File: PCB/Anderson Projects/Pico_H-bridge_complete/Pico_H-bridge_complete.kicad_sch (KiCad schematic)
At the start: 43 parts, among them J1 Screw_Terminal_01x9, J2 Motor Connector, J3 Screw_Terminal_01x02, SW1 SW_DIP_x01, U1 Pico, U11 MCP6001R, U5 OPA4197

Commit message: Gerber files for Pico_H-bridge_complete v1 generated
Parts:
- removed TP10: B, TestPoint:TestPoint_Plated_Hole_D2.0mm, symbol Connector:TestPoint
- removed TP7: Limit, TestPoint:TestPoint_Plated_Hole_D2.0mm, symbol Connector:TestPoint
- removed TP8: Home, TestPoint:TestPoint_Plated_Hole_D2.0mm, symbol Connector:TestPoint
- removed TP9: A, TestPoint:TestPoint_Plated_Hole_D2.0mm, symbol Connector:TestPoint
- D1: footprint LED_SMD:LED_0603_1608Metric -> LED_SMD:LED_0805_2012Metric; LCSC C2286 -> C2296
- D2: footprint LED_SMD:LED_0603_1608Metric -> LED_SMD:LED_0805_2012Metric; LCSC C2290 -> C34499
- J1: footprint TerminalBlock_Phoenix:TerminalBlock_Phoenix_PT-1,5-10-5.0-H_1x10_P5.00mm_Horizontal -> TerminalBlock_Phoenix:TerminalBlock_Phoenix_PT-1,5-9-5.0-H_1x09_P5.00mm_Horizontal
- R1, R2: footprint Resistor_SMD:R_0603_1608Metric -> Resistor_SMD:R_0805_2012Metric_Pad1.20x1.40mm_HandSolder
- R10, R4, R6: footprint Resistor_SMD:R_0603_1608Metric -> Resistor_SMD:R_0805_2012Metric_Pad1.20x1.40mm_HandSolder; LCSC C23018 -> C17614
- R11, R17: footprint Resistor_SMD:R_0603_1608Metric -> Resistor_SMD:R_0805_2012Metric_Pad1.20x1.40mm_HandSolder; LCSC C23186 -> C27834
- R12, R13, R15, R16, R18, R19: footprint Resistor_SMD:R_0603_1608Metric -> Resistor_SMD:R_0805_2012Metric_Pad1.20x1.40mm_HandSolder; LCSC C25804 -> C17414
- R14: footprint Resistor_SMD:R_0603_1608Metric -> Resistor_SMD:R_0805_2012Metric_Pad1.20x1.40mm_HandSolder; LCSC C25819 -> C17713
- R20, R21: footprint Resistor_SMD:R_0603_1608Metric -> Resistor_SMD:R_0805_2012Metric_Pad1.20x1.40mm_HandSolder; LCSC C22978 -> C26010
- R24: footprint Resistor_SMD:R_0603_1608Metric -> Resistor_SMD:R_0805_2012Metric_Pad1.20x1.40mm_HandSolder; LCSC C4260 -> C17767
- R25: footprint Resistor_SMD:R_0603_1608Metric -> Resistor_SMD:R_0805_2012Metric_Pad1.20x1.40mm_HandSolder; LCSC C22797 -> C17455
- R3, R5: footprint Resistor_SMD:R_0603_1608Metric -> Resistor_SMD:R_0805_2012Metric_Pad1.20x1.40mm_HandSolder; LCSC C4177 -> C17398
- U11: LCSC (none) -> C154973

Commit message: Anderson Motor Interface Board v2 complete and ordered.
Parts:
- removed D14: 5.1V, Diode_SMD:D_SOD-323, symbol Diode:Z1SMAxxx
- added R32: 82k, Resistor_SMD:R_0805_2012Metric_Pad1.20x1.40mm_HandSolder, symbol Device:R_US
- added R33, R34: 22k, Resistor_SMD:R_0805_2012Metric_Pad1.20x1.40mm_HandSolder, symbol Device:R_Small_US
- D1: LCSC C2296 -> C2295
- J1: footprint TerminalBlock_Phoenix:TerminalBlock_Phoenix_PT-1,5-9-5.0-H_1x09_P5.00mm_Horizontal -> TerminalBlock_Phoenix:TerminalBlock_Phoenix_PT-1,5-10-5.0-H_1x10_P5.00mm_Horizontal; symbol Connector:Screw_Terminal_01x09 -> Connector:Screw_Terminal_01x10
- R1, R2: value 330Ω -> 330
- R10: value 3.9k -> 82k; LCSC C17614 -> C17840
- R20, R21: value 3.3kΩ -> 3.3k
- R3, R5: value 1.8kΩ -> 1.8k
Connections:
- net Analog Position: now also J1.7 (Pin_7); no longer J1.6 (Pin_6)
- net Analog Position x10: now also J1.6 (Pin_6); no longer J1.5 (Pin_5)
- net Analog Speed: now also J1.8 (Pin_8); no longer J1.7 (Pin_7)
- net Fwd/Rev: now also R34.2
- net GND: now also J1.9 (Pin_9), R33.1, R34.1; no longer J1.8 (Pin_8)
- net at J1.2 (Pin_2): now also R32.1; no longer R25.2
- net at J1.3 (Pin_3): now also R25.2; no longer R4.1
- net at J1.4 (Pin_4): now also R4.1; no longer R6.1
- net at D5.2 (A): now also J1.10 (Pin_10); no longer J1.9 (Pin_9)
- new net: J1.5 (Pin_5), R6.1
- new net External PWM: R32.2, R33.2

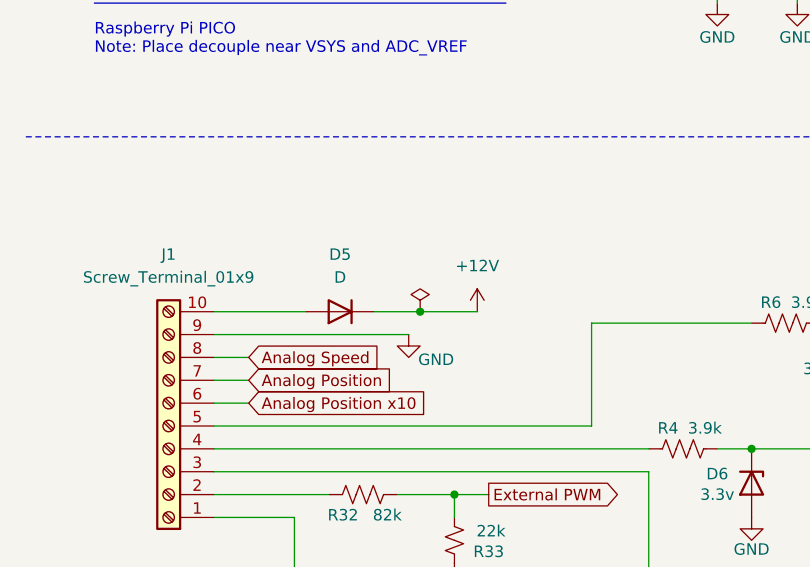
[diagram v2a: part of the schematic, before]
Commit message: Anderson Motor Interface Board v3. - Bengal eyes LED for both directions - heatsink pads on back of board - DIN rail mount Added Heater Box Schematic files in Documentation
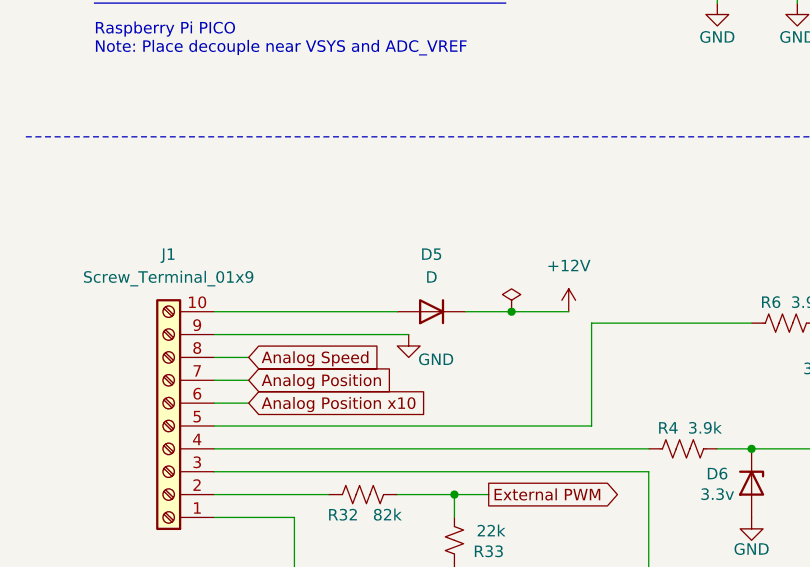
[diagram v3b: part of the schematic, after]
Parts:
- D1: LCSC C2295 -> C84256
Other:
- moved on the sheet: D5
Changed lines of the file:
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@@
 	)
 	(junction
-		(at 54.61 130.81)
+		(at 64.77 130.81)
 		(diameter 0)
 		(color 0 0 0 0)
@@
 	(wire
 		(pts
-			(xy 49.53 130.81) (xy 54.61 130.81)
+			(xy 59.69 130.81) (xy 64.77 130.81)
 		)
 		(stroke
@@
 	(wire
 		(pts
-			(xy 31.75 130.81) (xy 41.91 130.81)
+			(xy 31.75 130.81) (xy 52.07 130.81)
 		)
 		(stroke
@@
 	(wire
 		(pts
-			(xy 54.61 130.81) (xy 60.96 130.81)
+			(xy 64.77 130.81) (xy 71.12 130.81)
 		)
 		(stroke
@@
 	(symbol
 		(lib_id "power:PWR_FLAG")
-		(at 54.61 130.81 0)
+		(at 64.77 130.81 0)
 		(unit 1)
 		(exclude_from_sim no)
@@
 		(fields_autoplaced yes)
 		(property "Reference" "#FLG01"
-			(at 54.61 128.905 0)
+			(at 64.77 128.905 0)
 			(effects
 				(font
@@
 		)
 		(property "Value" "PWR_FLAG"
-			(at 54.61 125.73 0)
+			(at 64.77 125.73 0)
 			(effects
 				(font
@@
 		)
 		(property "Footprint" ""
-			(at 54.61 130.81 0)
+			(at 64.77 130.81 0)
 			(effects
 				(font
@@
 		)
 		(property "Datasheet" "~"
-			(at 54.61 130.81 0)
+			(at 64.77 130.81 0)
 			(effects
 				(font
@@
 		)
 		(property "Description" "Special symbol for telling ERC where power comes from"
-			(at 54.61 130.81 0)
+			(at 64.77 130.81 0)
 			(effects
 				(font
@@
 	(symbol
 		(lib_id "Device:D")
-		(at 45.72 130.81 180)
+		(at 55.88 130.81 180)
 		(unit 1)
 		(exclude_from_sim no)
@@
 		(fields_autoplaced yes)
 		(property "Reference" "D5"
-			(at 45.72 124.46 0)
+			(at 55.88 124.46 0)
 			(effects
 				(font
@@
 		)
 		(property "Value" "D"
-			(at 45.72 127 0)
+			(at 55.88 127 0)
 			(effects
 				(font
@@
 		)
 		(property "Footprint" "Diode_SMD:D_SMA"
-			(at 45.72 130.81 0)
+			(at 55.88 130.81 0)
 			(effects
 				(font
@@
 		)
 		(property "Datasheet" "https://jlcpcb.com/partdetail/mdd_microdiode_semiconductor-SS34/C8678"
-			(at 45.72 130.81 0)
+			(at 55.88 130.81 0)
 			(effects
 				(font
@@
 		)
 		(property "Description" "C8678 - protection diode"
-			(at 45.72 130.81 0)
+			(at 55.88 130.81 0)
 			(effects
 				(font
@@
 		)
 		(property "Sim.Device" "D"
-			(at 45.72 130.81 0)
+			(at 55.88 130.81 0)
 			(effects
 				(font
@@
 		)
 		(property "Sim.Pins" "1=K 2=A"
-			(at 45.72 130.81 0)
+			(at 55.88 130.81 0)
 			(effects
 				(font
@@
 		)
 		(property "LCSC" "C8678"
-			(at 45.72 130.81 0)
+			(at 55.88 130.81 0)
 			(effects
 				(font
@@
 			)
 		)
-		(property "Datasheet" "https://jlcpcb.com/partdetail/XkbConnection-DSIC01LSP/C600988"
+		(property "Datasheet" "~"
 			(at 24.13 67.31 0)
 			(effects
@@
 	(symbol
 		(lib_id "power:+12V")
-		(at 60.96 130.81 0)
+		(at 71.12 130.81 0)
 		(unit 1)
 		(exclude_from_sim no)
@@
 		(fields_autoplaced yes)
 		(property "Reference" "#PWR05"
-			(at 60.96 134.62 0)
+			(at 71.12 134.62 0)
 			(effects
 				(font
@@
 		)
 		(property "Value" "+12V"
-			(at 60.96 125.73 0)
+			(at 71.12 125.73 0)
 			(effects
 				(font
@@
 		)
 		(property "Footprint" ""
-			(at 60.96 130.81 0)
+			(at 71.12 130.81 0)
 			(effects
 				(font
@@
 		)
 		(property "Datasheet" ""
-			(at 60.96 130.81 0)
+			(at 71.12 130.81 0)
 			(effects
 				(font
@@
 		)
 		(property "Description" "Power symbol creates a global label with name \"+Motor_Sup\""
-			(at 60.96 130.81 0)
+			(at 71.12 130.81 0)
 			(effects
 				(font
@@
 			)
 		)
-		(property "Datasheet" "https://jlcpcb.com/partdetail/Hubei_KentoElec-KT0805R/C2295"
+		(property "Datasheet" "https://jlcpcb.com/partdetail/85425-NCD0805R1/C84256"
 			(at 87.63 91.44 90)
 			(effects
@@
 			)
 		)
-		(property "LCSC" "C2295"
+		(property "LCSC" "C84256"
 			(at 87.63 91.44 0)
 			(effects
